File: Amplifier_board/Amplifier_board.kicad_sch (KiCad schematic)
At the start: 15 parts, among them J1 Screw Terminal, J2 Screw Terminal, J3 Screw Terminal, J4 Screw Terminal, J5 Screw Terminal, J6 Screw Terminal, J7 A-DF_09_A_KG-T4S

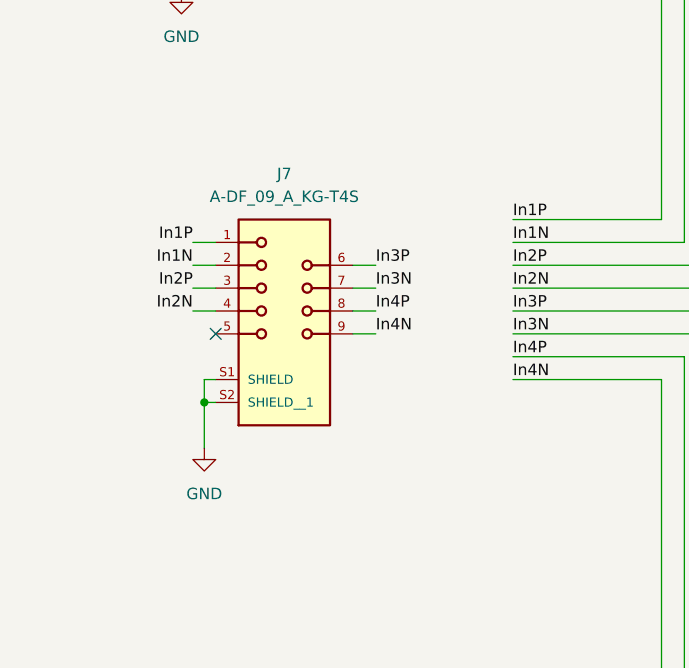
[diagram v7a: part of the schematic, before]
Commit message: Updated ribbon connector on amp board
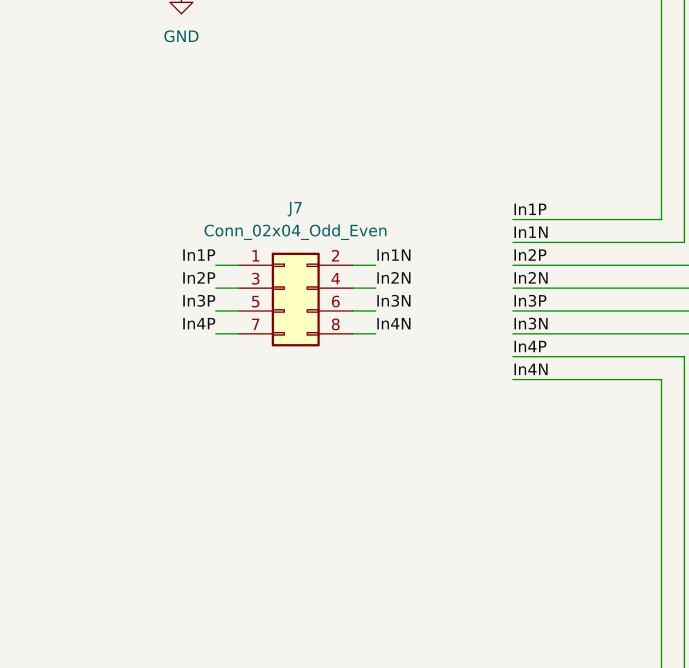
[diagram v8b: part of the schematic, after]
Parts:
- removed J7: A-DF_09_A_KG-T4S, project_lib:ASSMANN_A-DF_09_A_KG-T4S, symbol project_lib:A-DF_09_A_KG-T4S
- added J7: Conn_02x04_Odd_Even, project_lib:BHR-08-VUA, symbol Connector_Generic:Conn_02x04_Odd_Even
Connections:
- net In1N: now also J7.2 (Pin_2)
- net In1P: now also J7.1 (Pin_1)
- net In2N: now also J7.4 (Pin_4)
- net In2P: now also J7.3 (Pin_3)
- net In3N: now also J7.6 (Pin_6)
- net In3P: now also J7.5 (Pin_5)
- net In4N: now also J7.8 (Pin_8)
- net In4P: now also J7.7 (Pin_7)
- no-connect marks 1 -> 0
